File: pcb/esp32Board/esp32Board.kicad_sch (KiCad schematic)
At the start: 30 parts, among them J1 ESPProgJTAG_RX, J10 USB_C_Receptacle_USB2.0, J2 ESPProg_RX, J3 ESPProgUART_RX, J4 CAN, J5 UART2, J6 I2C, J7 IO, J8 PWR, J9 GND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

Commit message: PCB Update
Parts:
- C1: LCSC (none) -> C1591
- C2: value 20uF -> 22uF
- C5, C6: LCSC (none) -> C14664
- D2: LCSC C124187 -> C8678
- R2, R3, R8, R9: footprint Capacitor_SMD:C_0603_1608Metric -> Resistor_SMD:R_0603_1608Metric; LCSC (none) -> C429617
- R4: value 2k -> 100k; LCSC C226705 -> (none)
- R5: LCSC C429667 -> C429617
- SW1: LCSC (none) -> C557592
- U2: LCSC (none) -> C2892669
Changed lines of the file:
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@@
+      (effects (font (size 1.27 1.27)) hide)
+    )
+    (property "LCSC" "C557592" (id 4) (at 99.568 20.066 0)
       (effects (font (size 1.27 1.27)) hide)
     )
@@
       (effects (font (size 1.27 1.27)) hide)
     )
+    (property "LCSC" "C1591" (id 4) (at 19.431 28.956 0)
+      (effects (font (size 1.27 1.27)) hide)
+    )
     (pin "1")
     (pin "2")
@@
     (in_bom yes) (on_board yes)
     (property "Reference" "C2" (id 0) (at 53.594 15.24 90))
-    (property "Value" "20uF" (id 1) (at 53.594 21.9909 90))
+    (property "Value" "22uF" (id 1) (at 53.594 21.9909 90))
     (property "Footprint" "Capacitor_SMD:C_0603_1608Metric" (id 2) (at 57.404 19.6342 0)
       (effects (font (size 1.27 1.27)) hide)
@@
       (effects (font (size 1.27 1.27)) (justify left))
     )
-    (property "Value" "2k" (id 1) (at 239.141 30.607 0)
+    (property "Value" "100k" (id 1) (at 239.141 30.607 0)
       (effects (font (size 1.27 1.27)) (justify left))
     )
@@
       (effects (font (size 1.27 1.27)) hide)
     )
-    (property "LCSC" "C226705" (id 4) (at 237.363 29.464 0)
+    (property "LCSC" "" (id 4) (at 237.363 29.464 0)
       (effects (font (size 1.27 1.27)) hide)
     )
@@
       (effects (font (size 1.27 1.27)) hide)
     )
-    (property "LCSC" "C429667" (id 4) (at 183.261 97.409 0)
+    (property "LCSC" "C429617" (id 4) (at 183.261 97.409 0)
       (effects (font (size 1.27 1.27)) hide)
     )
@@
     (property "Reference" "R2" (id 0) (at 91.567 31.496 90))
     (property "Value" "0" (id 1) (at 91.567 33.655 90))
-    (property "Footprint" "Capacitor_SMD:C_0603_1608Metric" (id 2) (at 91.567 35.433 90)
+    (property "Footprint" "Resistor_SMD:R_0603_1608Metric" (id 2) (at 91.567 35.433 90)
       (effects (font (size 1.27 1.27)) hide)
     )
     (property "Datasheet" "~" (id 3) (at 91.567 33.655 0)
+      (effects (font (size 1.27 1.27)) hide)
+    )
+    (property "LCSC" "C429617" (id 4) (at 91.567 33.655 0)
       (effects (font (size 1.27 1.27)) hide)
     )
@@
     )
     (property "Datasheet" "~" (id 3) (at 270.383 29.464 0)
+      (effects (font (size 1.27 1.27)) hide)
+    )
+    (property "LCSC" "C14664" (id 4) (at 270.383 29.464 0)
       (effects (font (size 1.27 1.27)) hide)
     )
@@
     (property "Reference" "R9" (id 0) (at 118.999 119.761 90))
     (property "Value" "0" (id 1) (at 118.999 117.602 90))
-    (property "Footprint" "Capacitor_SMD:C_0603_1608Metric" (id 2) (at 118.999 115.824 90)
+    (property "Footprint" "Resistor_SMD:R_0603_1608Metric" (id 2) (at 118.999 115.824 90)
       (effects (font (size 1.27 1.27)) hide)
     )
     (property "Datasheet" "~" (id 3) (at 118.999 117.602 0)
+      (effects (font (size 1.27 1.27)) hide)
+    )
+    (property "LCSC" "C429617" (id 4) (at 118.999 117.602 0)
       (effects (font (size 1.27 1.27)) hide)
     )
@@
       (effects (font (size 1.27 1.27)) hide)
     )
+    (property "LCSC" "C14664" (id 4) (at 248.539 29.464 0)
+      (effects (font (size 1.27 1.27)) hide)
+    )
     (pin "1")
     (pin "2")
@@
       (effects (font (size 1.27 1.27)) hide)
     )
+    (property "LCSC" "C2892669" (id 4) (at 260.223 25.654 0)
+      (effects (font (size 1.27 1.27)) hide)
+    )
     (pin "1")
     (pin "2")
@@
       (effects (font (size 1.27 1.27)) hide)
     )
-    (property "LCSC" "C124187" (id 4) (at 209.931 55.499 0)
+    (property "LCSC" "C8678" (id 4) (at 209.931 55.499 0)
       (effects (font (size 1.27 1.27)) hide)
     )
@@
     (property "Reference" "R8" (id 0) (at 118.999 114.808 90))
     (property "Value" "0" (id 1) (at 118.999 112.649 90))
-    (property "Footprint" "Capacitor_SMD:C_0603_1608Metric" (id 2) (at 118.999 110.871 90)
+    (property "Footprint" "Resistor_SMD:R_0603_1608Metric" (id 2) (at 118.999 110.871 90)
       (effects (font (size 1.27 1.27)) hide)
     )
     (property "Datasheet" "~" (id 3) (at 118.999 112.649 0)
+      (effects (font (size 1.27 1.27)) hide)
+    )
+    (property "LCSC" "C429617" (id 4) (at 118.999 112.649 0)
       (effects (font (size 1.27 1.27)) hide)
     )
@@
     (property "Reference" "R3" (id 0) (at 91.567 38.354 90))
     (property "Value" "0" (id 1) (at 91.567 36.195 90))
-    (property "Footprint" "Capacitor_SMD:C_0603_1608Metric" (id 2) (at 91.567 34.417 90)
+    (property "Footprint" "Resistor_SMD:R_0603_1608Metric" (id 2) (at 91.567 34.417 90)
       (effects (font (size 1.27 1.27)) hide)
     )
     (property "Datasheet" "~" (id 3) (at 91.567 36.195 0)
+      (effects (font (size 1.27 1.27)) hide)
+    )
+    (property "LCSC" "C429617" (id 4) (at 91.567 36.195 0)
       (effects (font (size 1.27 1.27)) hide)
     )
@@
     )
     (path "/32d4c26d-1b77-483f-999b-04b4e8bb7704"
-      (reference "C2") (unit 1) (value "20uF") (footprint "Capacitor_SMD:C_0603_1608Metric")
+      (reference "C2") (unit 1) (value "22uF") (footprint "Capacitor_SMD:C_0603_1608Metric")
     )
     (path "/acdeb7b0-b0df-4e49-b5ec-5440c51ce459"
@@
     )
     (path "/6403a8c2-1fa1-4fc2-aee4-02162bc51de7"
-      (reference "R2") (unit 1) (value "0") (footprint "Capacitor_SMD:C_0603_1608Metric")
+      (reference "R2") (unit 1) (value "0") (footprint "Resistor_SMD:R_0603_1608Metric")
     )
     (path "/d6e79343-c4e1-4642-8368-c7043988c28c"
-      (reference "R3") (unit 1) (value "0") (footprint "Capacitor_SMD:C_0603_1608Metric")
+      (reference "R3") (unit 1) (value "0") (footprint "Resistor_SMD:R_0603_1608Metric")
     )
     (path "/5ad7721f-6bbc-40fa-8d8b-56c0803acef3"
-      (reference "R4") (unit 1) (value "2k") (footprint "Resistor_SMD:R_0603_1608Metric")
+      (reference "R4") (unit 1) (value "100k") (footprint "Resistor_SMD:R_0603_1608Metric")
     )
     (path "/5b68d766-6bf6-4df2-a453-4a4b7ecbcee5"
@@
     )
     (path "/b65b8216-072f-4a68-8a57-be85e2731dc0"
-      (reference "R8") (unit 1) (value "0") (footprint "Capacitor_SMD:C_0603_1608Metric")
+      (reference "R8") (unit 1) (value "0") (footprint "Resistor_SMD:R_0603_1608Metric")
     )
     (path "/806319ab-bfae-4fcb-b241-6847723975e9"
-      (reference "R9") (unit 1) (value "0") (footprint "Capacitor_SMD:C_0603_1608Metric")
+      (reference "R9") (unit 1) (value "0") (footprint "Resistor_SMD:R_0603_1608Metric")
     )
     (path "/09825ec2-075d-4df2-a161-71d596d8dec3"

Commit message: PCB V0.2
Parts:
- removed J2: ESPProg_RX, Connector_Molex:Molex_CLIK-Mate_502382-1070_1x10-1MP_P1.25mm_Vertical, symbol KisonNew:ESPProg_RX
- removed J7: IO, Connector_PinHeader_2.54mm:PinHeader_1x08_P2.54mm_Vertical, symbol Connector:Conn_01x08_Male
- removed R9: 0, Resistor_SMD:R_0603_1608Metric, symbol Device:R
- added D3: LED, LED_SMD:LED_0603_1608Metric, symbol Device:LED
- added J11: Conn_01x14_Female, Connector_PinHeader_2.54mm:PinHeader_1x14_P2.54mm_Vertical, symbol Connector:Conn_01x14_Female
- added J7: InputOnly, Connector_PinHeader_2.54mm:PinHeader_1x04_P2.54mm_Vertical, symbol Connector:Conn_01x04_Male
- added SW2, SW3, SW4: SW_Push_SPDT, KisonNew:0603JumperP3, symbol Switch:SW_Push_SPDT
- R4: value 100k -> 10k
- R8: value 0 -> 10k; LCSC C429617 -> (none)
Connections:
- net +3V3: now also SW2.3 (C), SW3.3 (C), SW4.1 (A)
- net EXT_5V: now also SW2.1 (A), SW4.3 (C)
- net GND: now also D3.1 (K), J11.13 (Pin_13), SW3.1 (A)
- net IO18: now also J11.5 (Pin_5), J11.8 (Pin_8)
- net IO19: now also J11.4 (Pin_4)
- net IO23: now also J11.2 (Pin_2), J11.6 (Pin_6)
- net IO27: now also J11.12 (Pin_12)
- net IO32: now also J11.10 (Pin_10)
- net IO33: now also J11.11 (Pin_11)
- net IO34: now also J7.2 (Pin_2)
- net IO5: now also J11.3 (Pin_3), J11.9 (Pin_9)
- net IO36: now reaches U1.4 (SENSOR_VP)
- net IO36: now also J7.4 (Pin_4)
- net IO39: now reaches U1.5 (SENSOR_VN)
- net IO39: now also J7.3 (Pin_3)
- net IO35: now reaches U1.7 (IO35)
- net IO35: now also J7.1 (Pin_1)
- net CAN_VCC: no longer names the net of J4.1 (Pin_1)
- net CAN_VCC: now also SW2.2 (B); no longer R8.2
- new net: J11.14 (Pin_14), SW4.2 (B)
- new net: J11.7 (Pin_7), SW3.2 (B)
- new net: D3.2 (A), R8.2
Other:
- moved on the sheet: J4

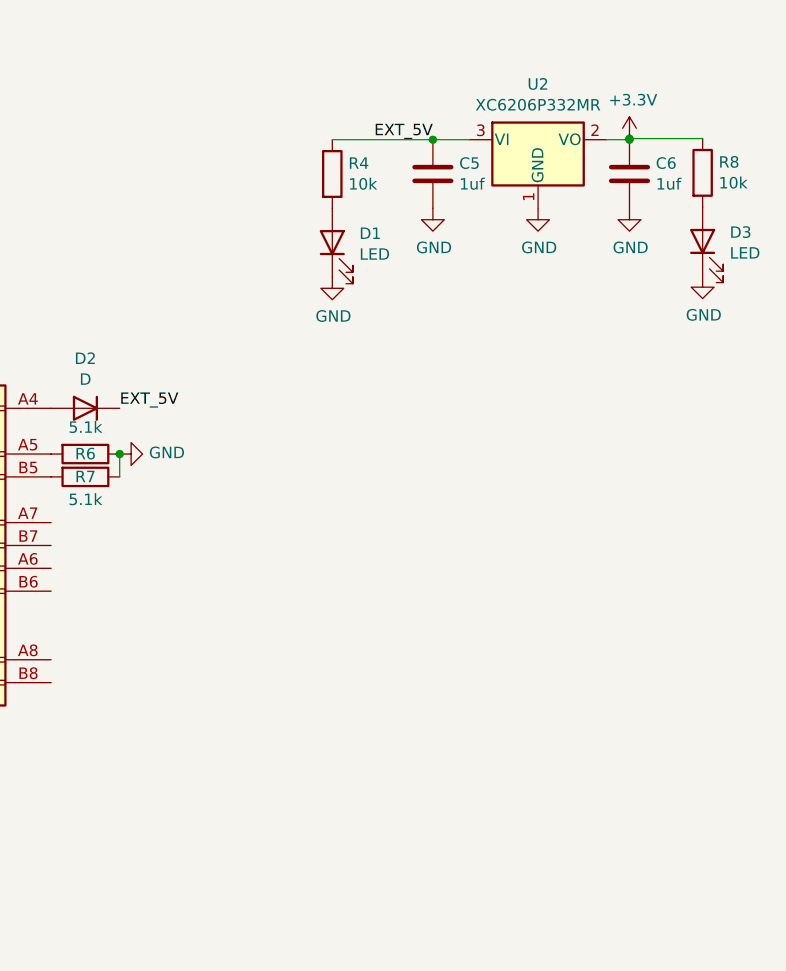
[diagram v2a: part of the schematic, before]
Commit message: Use XC6209 instead of trash XC6206
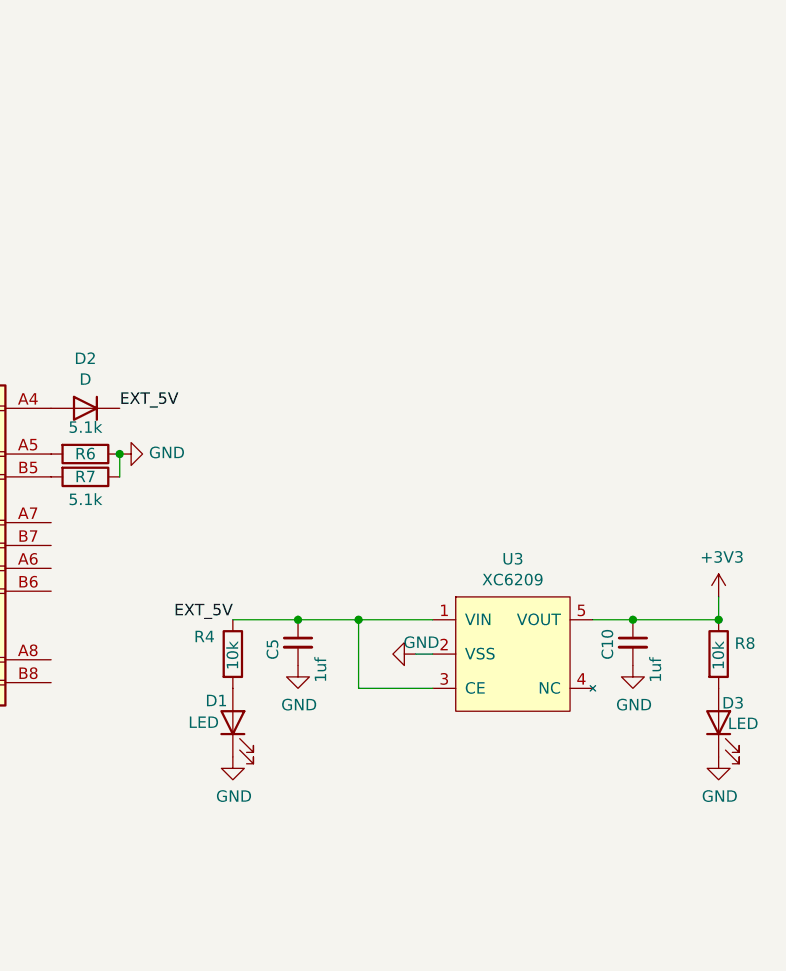
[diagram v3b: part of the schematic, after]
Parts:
- removed C5, C6: 1uf, Capacitor_SMD:C_0603_1608Metric, symbol Device:C
- removed U2: XC6206P332MR, Package_TO_SOT_SMD:SOT-23, symbol Regulator_Linear:XC6206PxxxMR
- added C10, C5: 1uf, Capacitor_SMD:C_0603_1608Metric, symbol Device:C_Small
- added U3: XC6209, Package_TO_SOT_SMD:SOT-23-5, symbol open-Smartwatch:XC6209
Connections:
- net +3V3: now also C10.1, U3.5 (VOUT)
- net EXT_5V: now also C5.1, U3.1 (VIN), U3.3 (CE)
- net GND: now also C10.2, C5.2, U3.2 (VSS)
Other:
- moved on the sheet: D1, D3, R4, R8

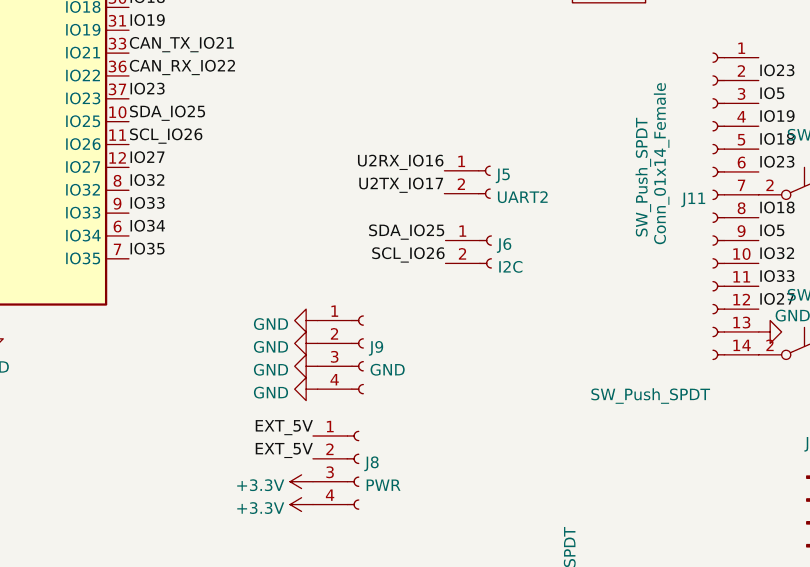
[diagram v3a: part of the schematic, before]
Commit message: Fix I2C Pull Up
https://github.com/espressif/arduino-esp32/issues/3424 Damn why not design it strong enough so bad
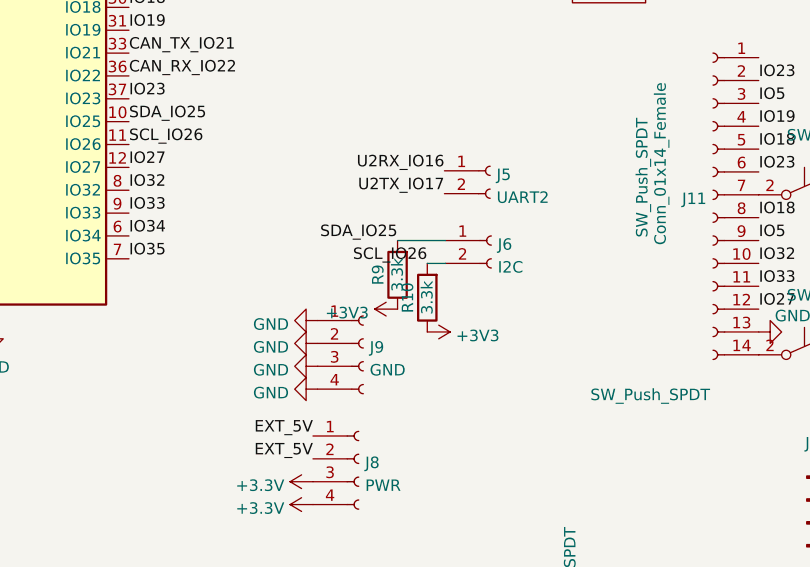
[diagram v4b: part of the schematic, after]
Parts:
- added R10, R9: 3.3k, Resistor_SMD:R_0603_1608Metric, symbol Device:R
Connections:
- net +3V3: now also R10.1, R9.1
- net SCL_IO26: now also R10.2
- net SDA_IO25: now also R9.2
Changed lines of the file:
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@@
+    (stroke (width 0) (type default) (color 0 0 0 0))
+  )
+  (wire (pts (xy 105.791 89.281) (xy 107.823 89.281))
+    (stroke (width 0) (type default) (color 0 0 0 0))
+  )
+  (wire (pts (xy 102.489 86.741) (xy 107.823 86.741))
     (stroke (width 0) (type default) (color 0 0 0 0))
   )
@@
     (effects (font (size 1.27 1.27)) (justify left bottom))
   )
-  (label "SCL_IO26" (at 107.823 89.281 180)
+  (label "SCL_IO26" (at 105.791 89.281 180)
     (effects (font (size 1.27 1.27)) (justify right bottom))
   )
-  (label "SDA_IO25" (at 107.823 86.741 180)
+  (label "SDA_IO25" (at 102.489 86.741 180)
     (effects (font (size 1.27 1.27)) (justify right bottom))
   )
@@
     (pin "1")
   )
+  (symbol (lib_id "power:+3V3") (at 102.489 94.361 90) (unit 1)
+    (in_bom yes) (on_board yes) (fields_autoplaced)
+    (property "Reference" "#PWR0116" (id 0) (at 106.299 94.361 0)
+      (effects (font (size 1.27 1.27)) hide)
+    )
+    (property "Value" "+3V3" (id 1) (at 99.314 94.7948 90)
+      (effects (font (size 1.27 1.27)) (justify left))
+    )
+    (property "Footprint" "" (id 2) (at 102.489 94.361 0)
+      (effects (font (size 1.27 1.27)) hide)
+    )
+    (property "Datasheet" "" (id 3) (at 102.489 94.361 0)
+      (effects (font (size 1.27 1.27)) hide)
+    )
+    (pin "1")
+  )
   (symbol (lib_id "open-Smartwatch:XC6209") (at 257.429 82.804 0) (unit 1)
     (in_bom yes) (on_board yes)
@@
     )
     (pin "1")
+  )
+  (symbol (lib_id "Device:R") (at 105.791 93.091 180) (unit 1)
+    (in_bom yes) (on_board yes)
+    (property "Reference" "R10" (id 0) (at 103.632 93.091 90))
+    (property "Value" "3.3k" (id 1) (at 105.791 93.091 90))
+    (property "Footprint" "Resistor_SMD:R_0603_1608Metric" (id 2) (at 107.569 93.091 90)
+      (effects (font (size 1.27 1.27)) hide)
+    )
+    (property "Datasheet" "~" (id 3) (at 105.791 93.091 0)
+      (effects (font (size 1.27 1.27)) hide)
+    )
+    (property "LCSC" "C429617" (id 4) (at 105.791 93.091 0)
+      (effects (font (size 1.27 1.27)) hide)
+    )
+    (pin "1")
+    (pin "2")
   )
   (symbol (lib_id "Device:C") (at 53.594 18.669 90) (mirror x) (unit 1)
@@
     (pin "1")
   )
+  (symbol (lib_id "Device:R") (at 102.489 90.551 180) (unit 1)
+    (in_bom yes) (on_board yes)
+    (property "Reference" "R9" (id 0) (at 100.33 90.551 90))
+    (property "Value" "3.3k" (id 1) (at 102.489 90.551 90))
+    (property "Footprint" "Resistor_SMD:R_0603_1608Metric" (id 2) (at 104.267 90.551 90)
+      (effects (font (size 1.27 1.27)) hide)
+    )
+    (property "Datasheet" "~" (id 3) (at 102.489 90.551 0)
+      (effects (font (size 1.27 1.27)) hide)
+    )
+    (property "LCSC" "C429617" (id 4) (at 102.489 90.551 0)
+      (effects (font (size 1.27 1.27)) hide)
+    )
+    (pin "1")
+    (pin "2")
+  )
   (symbol (lib_id "power:GND") (at 19.431 32.766 0) (unit 1)
     (in_bom yes) (on_board yes) (fields_autoplaced)
@@
     )
     (property "Datasheet" "" (id 3) (at 93.091 116.078 0)
+      (effects (font (size 1.27 1.27)) hide)
+    )
+    (pin "1")
+  )
+  (symbol (lib_id "power:+3V3") (at 105.791 96.901 270) (unit 1)
+    (in_bom yes) (on_board yes) (fields_autoplaced)
+    (property "Reference" "#PWR0117" (id 0) (at 101.981 96.901 0)
+      (effects (font (size 1.27 1.27)) hide)
+    )
+    (property "Value" "+3V3" (id 1) (at 108.966 97.3348 90)
+      (effects (font (size 1.27 1.27)) (justify left))
+    )
+    (property "Footprint" "" (id 2) (at 105.791 96.901 0)
+      (effects (font (size 1.27 1.27)) hide)
+    )
+    (property "Datasheet" "" (id 3) (at 105.791 96.901 0)
       (effects (font (size 1.27 1.27)) hide)
     )
@@
       (reference "#PWR0115") (unit 1) (value "+3V3") (footprint "")
     )
+    (path "/1af6b69a-9a5d-4fb8-925f-388b223153e6"
+      (reference "#PWR0116") (unit 1) (value "+3V3") (footprint "")
+    )
+    (path "/b086fbf5-a8ea-4f52-83a9-6d0d0b695f01"
+      (reference "#PWR0117") (unit 1) (value "+3V3") (footprint "")
+    )
     (path "/2137cba9-dcaf-471d-9ef5-3e5eb1727851"
       (reference "#PWR0118") (unit 1) (value "GND") (footprint "")
@@
       (reference "R8") (unit 1) (value "10k") (footprint "Resistor_SMD:R_0603_1608Metric")
     )
+    (path "/a2d3eb96-58a0-4346-af1e-78bb35a50430"
+      (reference "R9") (unit 1) (value "3.3k") (footprint "Resistor_SMD:R_0603_1608Metric")
+    )
+    (path "/30d02a7b-4068-41c4-9af0-f40acb1571ce"
+      (reference "R10") (unit 1) (value "3.3k") (footprint "Resistor_SMD:R_0603_1608Metric")
+    )
     (path "/09825ec2-075d-4df2-a161-71d596d8dec3"
